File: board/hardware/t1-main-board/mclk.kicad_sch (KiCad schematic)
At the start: 32 parts, among them U2401 SN74LVC1G57DCKR, U2402 TPS7A2031PDBVR, U2403 TPS7A2018PDBVR, U2404 SN74AUC1G74DCUR, U2405 SN74AUC1G74DCUR, Y2401 45.1584 MHz, Y2402 49.152 MHz

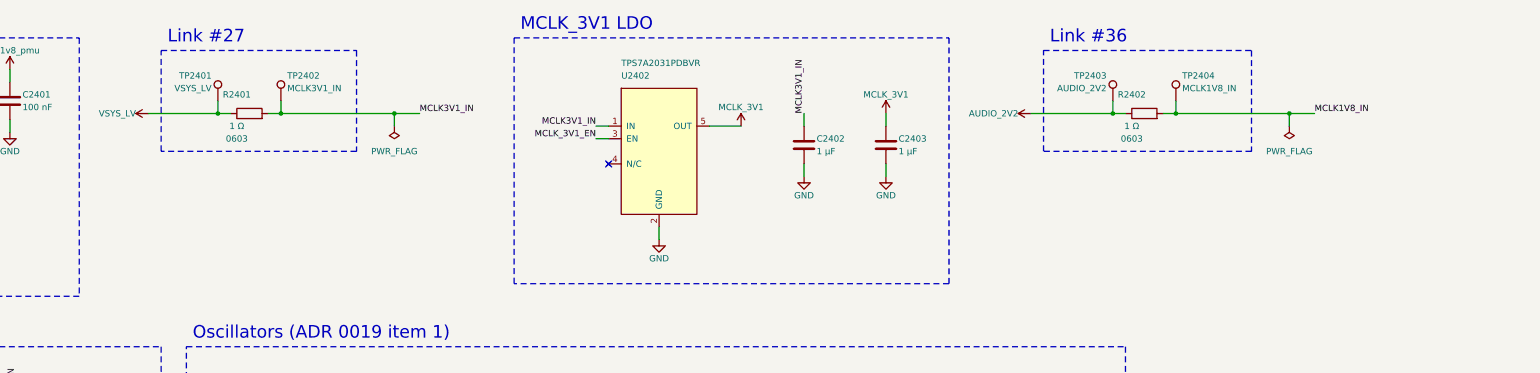
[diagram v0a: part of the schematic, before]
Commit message: Board: capture blk.current-monitors
Five INA236 on I2C1 (0x40-0x43, 0x48) with their shunts, per power tree
§4.12 and BOM v1 lines 54 and 136. The measured branches are rails of
their own (VSYS_SRC, VSYS_LV_AUDIO, VSYS_AUDIO, VSYS_LV_BL, VSYS_P5V1),
fed through the shunts on this sheet; the charger, audio, backlight and
5.1 V sheets take them. The root's layout may leave a stack level empty,
so the block sits under the notes; IC bboxes hold turned rail values;
passive rows hold a bottom rail's text.

Co-Authored-By: Claude Opus 5.5 <noreply@anthropic.com>
Claude-Session: https://claude.ai/code/session_01Ei262h3TpgY9vyfNLMi5Mn
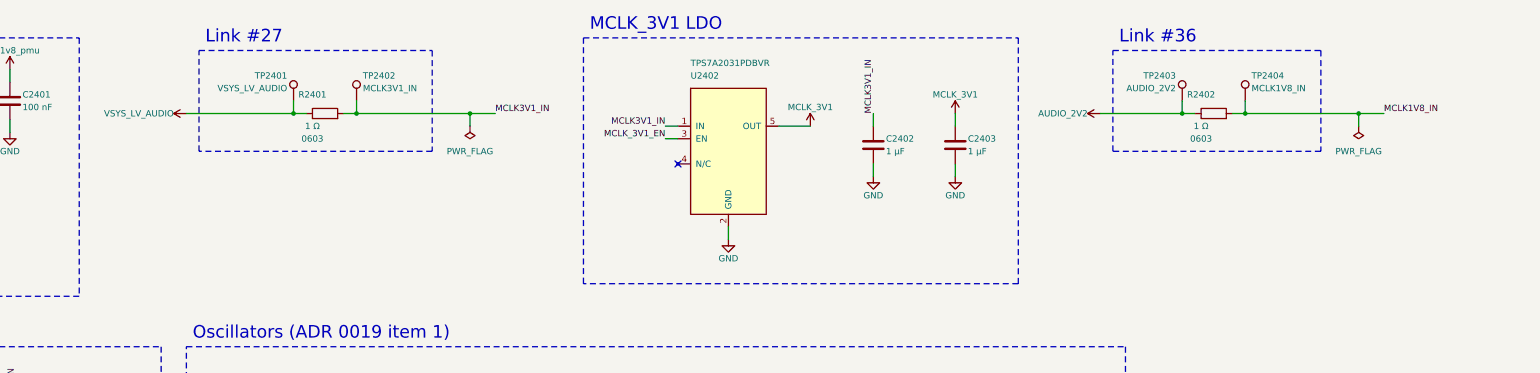
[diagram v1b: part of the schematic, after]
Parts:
- TP2401: value VSYS_LV -> VSYS_LV_AUDIO
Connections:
- net VSYS_LV renamed VSYS_LV_AUDIO
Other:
- moved on the sheet: C2402, C2403, R2401, R2402, TP2401, TP2402, TP2403, TP2404, U2402

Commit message: Board on libs v0.2.0: lower-case kebab vendor keys (HL-13)
The libs submodule moves to v0.2.0 (5f24483). Every library nickname in
the generator, the placement tool and the floorplan study follows the
key table (Texas_Instruments -> texas-instruments, OpenDAP_Device ->
opendap-generic, Rockchip and Rockchip_PMIC -> rockchip, ...); the
library tables are written from the files. Schematic and board
regenerated.

Checks: ERC 0 errors (warnings unchanged); DRC 0 errors, 605 warnings,
the same counts by type, schematic parity 0; every placement identical;
craft Q1 met; pcb tests pass; STEP export resolves every libs 3D model
(the 27 parts without a model are KiCad stock lands that have none).

Co-Authored-By: Claude Opus 5.5 <noreply@anthropic.com>
Claude-Session: https://claude.ai/code/session_01Ei262h3TpgY9vyfNLMi5Mn
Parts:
- U2401: footprint Texas_Instruments:Texas_DCK0006A_SC-70-6_1.25x2mm_P0.65mm -> texas-instruments:Texas_DCK0006A_SC-70-6_1.25x2mm_P0.65mm; symbol Texas_Instruments:SN74LVC1G57DCKR -> texas-instruments:SN74LVC1G57DCKR
- U2402: footprint Texas_Instruments:Texas_DBV0005A_SOT-23-5_1.6x2.9mm_P0.95mm -> texas-instruments:Texas_DBV0005A_SOT-23-5_1.6x2.9mm_P0.95mm; symbol Texas_Instruments:TPS7A2031PDBVR -> texas-instruments:TPS7A2031PDBVR
- U2403: footprint Texas_Instruments:Texas_DBV0005A_SOT-23-5_1.6x2.9mm_P0.95mm -> texas-instruments:Texas_DBV0005A_SOT-23-5_1.6x2.9mm_P0.95mm; symbol Texas_Instruments:TPS7A2018PDBVR -> texas-instruments:TPS7A2018PDBVR
- U2404, U2405: footprint Texas_Instruments:Texas_DCU0008A_VSSOP-8_2.3x2mm_P0.5mm -> texas-instruments:Texas_DCU0008A_VSSOP-8_2.3x2mm_P0.5mm; symbol Texas_Instruments:SN74AUC1G74DCUR -> texas-instruments:SN74AUC1G74DCUR
- Y2401: footprint NDK:Oscillator_SMD_NDK_NZ2520SDA-4Pin_2.5x2.0mm -> ndk:Oscillator_SMD_NDK_NZ2520SDA-4Pin_2.5x2.0mm; symbol NDK:NSC5083D-45.158M -> ndk:NSC5083D-45.158M
- Y2402: footprint NDK:Oscillator_SMD_NDK_NZ2520SDA-4Pin_2.5x2.0mm -> ndk:Oscillator_SMD_NDK_NZ2520SDA-4Pin_2.5x2.0mm; symbol NDK:NSC5083D-49.152M -> ndk:NSC5083D-49.152M
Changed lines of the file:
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@@
 (paper "A3")
 (title_block (title "Audio: master clocks") (date "2026-10-25") (rev "A") (company "The OpenDAP Project") (comment 1 "blk.mclk") (comment 2 "Two oscillators at twice the MCLK, their LDOs and interlock, one divider per DAC (ADR 0019)"))
-(symbol (lib_id "Texas_Instruments:SN74LVC1G57DCKR") (at 63.5 60.96 0) (unit 1) (body_style 1) (exclude_from_sim no) (in_bom yes) (on_board yes) (dnp no)
+(symbol (lib_id "texas-instruments:SN74LVC1G57DCKR") (at 63.5 60.96 0) (unit 1) (body_style 1) (exclude_from_sim no) (in_bom yes) (on_board yes) (dnp no)
   (property "Reference" "U2401" (at 64.77 45.72 0) (effects (font (size 1.27 1.27)) (justify left)))
   (property "Value" "SN74LVC1G57DCKR" (at 64.77 43.18 0) (effects (font (size 1.27 1.27)) (justify left)))
-  (property "Footprint" "Texas_Instruments:Texas_DCK0006A_SC-70-6_1.25x2mm_P0.65mm" (at 63.5 60.96 0) (effects (font (size 1.27 1.27))) (hide yes))
+  (property "Footprint" "texas-instruments:Texas_DCK0006A_SC-70-6_1.25x2mm_P0.65mm" (at 63.5 60.96 0) (effects (font (size 1.27 1.27))) (hide yes))
   (property "Datasheet" "https://www.ti.com/lit/ds/symlink/sn74lvc1g57.pdf" (at 63.5 60.96 0) (effects (font (size 1.27 1.27))) (hide yes))
   (property "Description" "Configurable multiple-function gate (AND, OR, NAND, NOR, XNOR, inverter, buffer by wiring), Schmitt-trigger inputs, 1.65-5.5 V, Ioff, SOT/SC-70-6 (DCK0006A)" (at 63.5 60.96 0) (effects (font (size 1.27 1.27))) (hide yes))
@@
   (instances (project "t1-main-board" (path "/7746052e-d7f9-59ad-ba73-bd2b74439529/d6f0155c-678f-5298-bf09-6ea7c0e72438/bff4696c-7e5a-50e5-8850-1d3e47ed608b" (reference "#FLG0019") (unit 1))))
 )
-(symbol (lib_id "Texas_Instruments:TPS7A2031PDBVR") (at 237.49 58.42 0) (unit 1) (body_style 1) (exclude_from_sim no) (in_bom yes) (on_board yes) (dnp no)
+(symbol (lib_id "texas-instruments:TPS7A2031PDBVR") (at 237.49 58.42 0) (unit 1) (body_style 1) (exclude_from_sim no) (in_bom yes) (on_board yes) (dnp no)
   (property "Reference" "U2402" (at 229.87 43.18 0) (effects (font (size 1.27 1.27)) (justify left)))
   (property "Value" "TPS7A2031PDBVR" (at 229.87 40.64 0) (effects (font (size 1.27 1.27)) (justify left)))
-  (property "Footprint" "Texas_Instruments:Texas_DBV0005A_SOT-23-5_1.6x2.9mm_P0.95mm" (at 237.49 58.42 0) (effects (font (size 1.27 1.27))) (hide yes))
+  (property "Footprint" "texas-instruments:Texas_DBV0005A_SOT-23-5_1.6x2.9mm_P0.95mm" (at 237.49 58.42 0) (effects (font (size 1.27 1.27))) (hide yes))
   (property "Datasheet" "https://www.ti.com/lit/ds/symlink/tps7a20.pdf" (at 237.49 58.42 0) (effects (font (size 1.27 1.27))) (hide yes))
   (property "Description" "LDO regulator, 300 mA, 3.1 V fixed, 7 uVrms noise, 95 dB PSRR at 1 kHz, active output discharge, SOT-23-5 (DBV0005A)" (at 237.49 58.42 0) (effects (font (size 1.27 1.27))) (hide yes))
@@
   (instances (project "t1-main-board" (path "/7746052e-d7f9-59ad-ba73-bd2b74439529/d6f0155c-678f-5298-bf09-6ea7c0e72438/bff4696c-7e5a-50e5-8850-1d3e47ed608b" (reference "#FLG0020") (unit 1))))
 )
-(symbol (lib_id "Texas_Instruments:TPS7A2018PDBVR") (at 64.77 120.65 0) (unit 1) (body_style 1) (exclude_from_sim no) (in_bom yes) (on_board yes) (dnp no)
+(symbol (lib_id "texas-instruments:TPS7A2018PDBVR") (at 64.77 120.65 0) (unit 1) (body_style 1) (exclude_from_sim no) (in_bom yes) (on_board yes) (dnp no)
   (property "Reference" "U2403" (at 57.15 105.41 0) (effects (font (size 1.27 1.27)) (justify left)))
   (property "Value" "TPS7A2018PDBVR" (at 57.15 102.87 0) (effects (font (size 1.27 1.27)) (justify left)))
-  (property "Footprint" "Texas_Instruments:Texas_DBV0005A_SOT-23-5_1.6x2.9mm_P0.95mm" (at 64.77 120.65 0) (effects (font (size 1.27 1.27))) (hide yes))
+  (property "Footprint" "texas-instruments:Texas_DBV0005A_SOT-23-5_1.6x2.9mm_P0.95mm" (at 64.77 120.65 0) (effects (font (size 1.27 1.27))) (hide yes))
   (property "Datasheet" "https://www.ti.com/lit/ds/symlink/tps7a20.pdf" (at 64.77 120.65 0) (effects (font (size 1.27 1.27))) (hide yes))
   (property "Description" "LDO regulator, 300 mA, 1.8 V fixed, 7 uVrms noise, 95 dB PSRR at 1 kHz, active output discharge, SOT-23-5 (DBV0005A)" (at 64.77 120.65 0) (effects (font (size 1.27 1.27))) (hide yes))
@@
 (rectangle (start 22.86 97.79) (end 123.19 147.32) (stroke (width 0) (type dash)) (fill (type none)))
 (text "MCLK_1V8 LDO (ADR 0019 item 3)" (exclude_from_sim no) (at 24.13 96.52 0) (effects (font (size 2.54 2.54)) (justify left bottom)))
-(symbol (lib_id "NDK:NSC5083D-45.158M") (at 170.18 125.73 0) (unit 1) (body_style 1) (exclude_from_sim no) (in_bom yes) (on_board yes) (dnp no)
+(symbol (lib_id "ndk:NSC5083D-45.158M") (at 170.18 125.73 0) (unit 1) (body_style 1) (exclude_from_sim no) (in_bom yes) (on_board yes) (dnp no)
   (property "Reference" "Y2401" (at 171.45 113.03 0) (effects (font (size 1.27 1.27)) (justify left)))
   (property "Value" "45.1584 MHz" (at 171.45 110.49 0) (effects (font (size 1.27 1.27)) (justify left)))
-  (property "Footprint" "NDK:Oscillator_SMD_NDK_NZ2520SDA-4Pin_2.5x2.0mm" (at 170.18 125.73 0) (effects (font (size 1.27 1.27))) (hide yes))
+  (property "Footprint" "ndk:Oscillator_SMD_NDK_NZ2520SDA-4Pin_2.5x2.0mm" (at 170.18 125.73 0) (effects (font (size 1.27 1.27))) (hide yes))
   (property "Datasheet" "https://www.ndk.com/images/products/catalog/c_NZ2520SDA_e.pdf" (at 170.18 125.73 0) (effects (font (size 1.27 1.27))) (hide yes))
   (property "Description" "45.158 MHz CMOS-output crystal clock oscillator, NZ2520SDA spec. NSC5083D (3.3 V, +/-50 ppm, -40 to +85 C), standby (three-state), 2.5 x 2.0 mm, 4 terminals" (at 170.18 125.73 0) (effects (font (size 1.27 1.27))) (hide yes))
@@
 (wire (pts (xy 182.88 125.73) (xy 186.69 125.73)) (stroke (width 0) (type default)))
 (wire (pts (xy 194.31 125.73) (xy 196.85 125.73)) (stroke (width 0) (type default)))
-(symbol (lib_id "NDK:NSC5083D-49.152M") (at 276.86 125.73 0) (unit 1) (body_style 1) (exclude_from_sim no) (in_bom yes) (on_board yes) (dnp no)
+(symbol (lib_id "ndk:NSC5083D-49.152M") (at 276.86 125.73 0) (unit 1) (body_style 1) (exclude_from_sim no) (in_bom yes) (on_board yes) (dnp no)
   (property "Reference" "Y2402" (at 278.13 113.03 0) (effects (font (size 1.27 1.27)) (justify left)))
   (property "Value" "49.152 MHz" (at 278.13 110.49 0) (effects (font (size 1.27 1.27)) (justify left)))
-  (property "Footprint" "NDK:Oscillator_SMD_NDK_NZ2520SDA-4Pin_2.5x2.0mm" (at 276.86 125.73 0) (effects (font (size 1.27 1.27))) (hide yes))
+  (property "Footprint" "ndk:Oscillator_SMD_NDK_NZ2520SDA-4Pin_2.5x2.0mm" (at 276.86 125.73 0) (effects (font (size 1.27 1.27))) (hide yes))
   (property "Datasheet" "https://www.ndk.com/images/products/catalog/c_NZ2520SDA_e.pdf" (at 276.86 125.73 0) (effects (font (size 1.27 1.27))) (hide yes))
   (property "Description" "49.152 MHz CMOS-output crystal clock oscillator, NZ2520SDA spec. NSC5083D (3.3 V, +/-50 ppm, -40 to +85 C), standby (three-state), 2.5 x 2.0 mm, 4 terminals" (at 276.86 125.73 0) (effects (font (size 1.27 1.27))) (hide yes))
@@
 (rectangle (start 22.86 158.75) (end 119.38 198.12) (stroke (width 0) (type dash)) (fill (type none)))
 (text "Pulls and bypass" (exclude_from_sim no) (at 24.13 157.48 0) (effects (font (size 2.54 2.54)) (justify left bottom)))
-(symbol (lib_id "Texas_Instruments:SN74AUC1G74DCUR") (at 158.75 186.69 0) (unit 1) (body_style 1) (exclude_from_sim no) (in_bom yes) (on_board yes) (dnp no)
+(symbol (lib_id "texas-instruments:SN74AUC1G74DCUR") (at 158.75 186.69 0) (unit 1) (body_style 1) (exclude_from_sim no) (in_bom yes) (on_board yes) (dnp no)
   (property "Reference" "U2404" (at 160.02 168.91 0) (effects (font (size 1.27 1.27)) (justify left)))
   (property "Value" "SN74AUC1G74DCUR" (at 160.02 166.37 0) (effects (font (size 1.27 1.27)) (justify left)))
-  (property "Footprint" "Texas_Instruments:Texas_DCU0008A_VSSOP-8_2.3x2mm_P0.5mm" (at 158.75 186.69 0) (effects (font (size 1.27 1.27))) (hide yes))
+  (property "Footprint" "texas-instruments:Texas_DCU0008A_VSSOP-8_2.3x2mm_P0.5mm" (at 158.75 186.69 0) (effects (font (size 1.27 1.27))) (hide yes))
   (property "Datasheet" "https://www.ti.com/lit/ds/symlink/sn74auc1g74.pdf" (at 158.75 186.69 0) (effects (font (size 1.27 1.27))) (hide yes))
   (property "Description" "Single positive-edge-triggered D-type flip-flop with clear and preset, AUC family, 0.8-2.7 V, 3.6 V-tolerant inputs, VSSOP-8 (DCU0008A)" (at 158.75 186.69 0) (effects (font (size 1.27 1.27))) (hide yes))
@@
 (wire (pts (xy 166.37 181.61) (xy 180.34 181.61)) (stroke (width 0) (type default)))
 (wire (pts (xy 187.96 181.61) (xy 190.5 181.61)) (stroke (width 0) (type default)))
-(symbol (lib_id "Texas_Instruments:SN74AUC1G74DCUR") (at 236.22 186.69 0) (unit 1) (body_style 1) (exclude_from_sim no) (in_bom yes) (on_board yes) (dnp no)
+(symbol (lib_id "texas-instruments:SN74AUC1G74DCUR") (at 236.22 186.69 0) (unit 1) (body_style 1) (exclude_from_sim no) (in_bom yes) (on_board yes) (dnp no)
   (property "Reference" "U2405" (at 237.49 168.91 0) (effects (font (size 1.27 1.27)) (justify left)))
   (property "Value" "SN74AUC1G74DCUR" (at 237.49 166.37 0) (effects (font (size 1.27 1.27)) (justify left)))
-  (property "Footprint" "Texas_Instruments:Texas_DCU0008A_VSSOP-8_2.3x2mm_P0.5mm" (at 236.22 186.69 0) (effects (font (size 1.27 1.27))) (hide yes))
+  (property "Footprint" "texas-instruments:Texas_DCU0008A_VSSOP-8_2.3x2mm_P0.5mm" (at 236.22 186.69 0) (effects (font (size 1.27 1.27))) (hide yes))
   (property "Datasheet" "https://www.ti.com/lit/ds/symlink/sn74auc1g74.pdf" (at 236.22 186.69 0) (effects (font (size 1.27 1.27))) (hide yes))
   (property "Description" "Single positive-edge-triggered D-type flip-flop with clear and preset, AUC family, 0.8-2.7 V, 3.6 V-tolerant inputs, VSSOP-8 (DCU0008A)" (at 236.22 186.69 0) (effects (font (size 1.27 1.27))) (hide yes))

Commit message: BOM v1.18 item 2: successors of the discontinued 1 uF 0402
GRM155R61A105KE15D is to be discontinued. 44 positions take
GRM155C71A105KE11D (1 uF 10 V X7S); the eight TPS7A20 positions take
GRM155R61C225KE11D (2.2 uF 16 V X5R) to keep the 0.47 uF effective
minimum with 10 % to spare at up to 3.8 V. Same land; sourcing pass.
Closes BOM §7 item 52; new item 55 lists the other capture parts outside
Murata's product data or near end of life.

Co-Authored-By: Claude Opus 5.5 <noreply@anthropic.com>
Claude-Session: https://claude.ai/code/session_01Ei262h3TpgY9vyfNLMi5Mn
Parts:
- C2402, C2403, C2404, C2405: value 1 µF -> 2.2 µF; MPN GRM155R61A105KE15D -> GRM155R61C225KE11D
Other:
- moved on the sheet: C2403, C2405, R2402, R2403, R2404, R2405, R2406, TP2403, TP2404, Y2401, Y2402
